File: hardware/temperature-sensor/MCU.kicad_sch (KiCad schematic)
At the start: 43 parts, among them J4 ARM-JTAG-SWD, Q2 DMN3404L, Q3 DMN3404L, Q4 DMN3404L, U1 STM32F407V_E-G_Tx, U4 AT24C512C, Y1 CX2016FB25000C0FZZH1

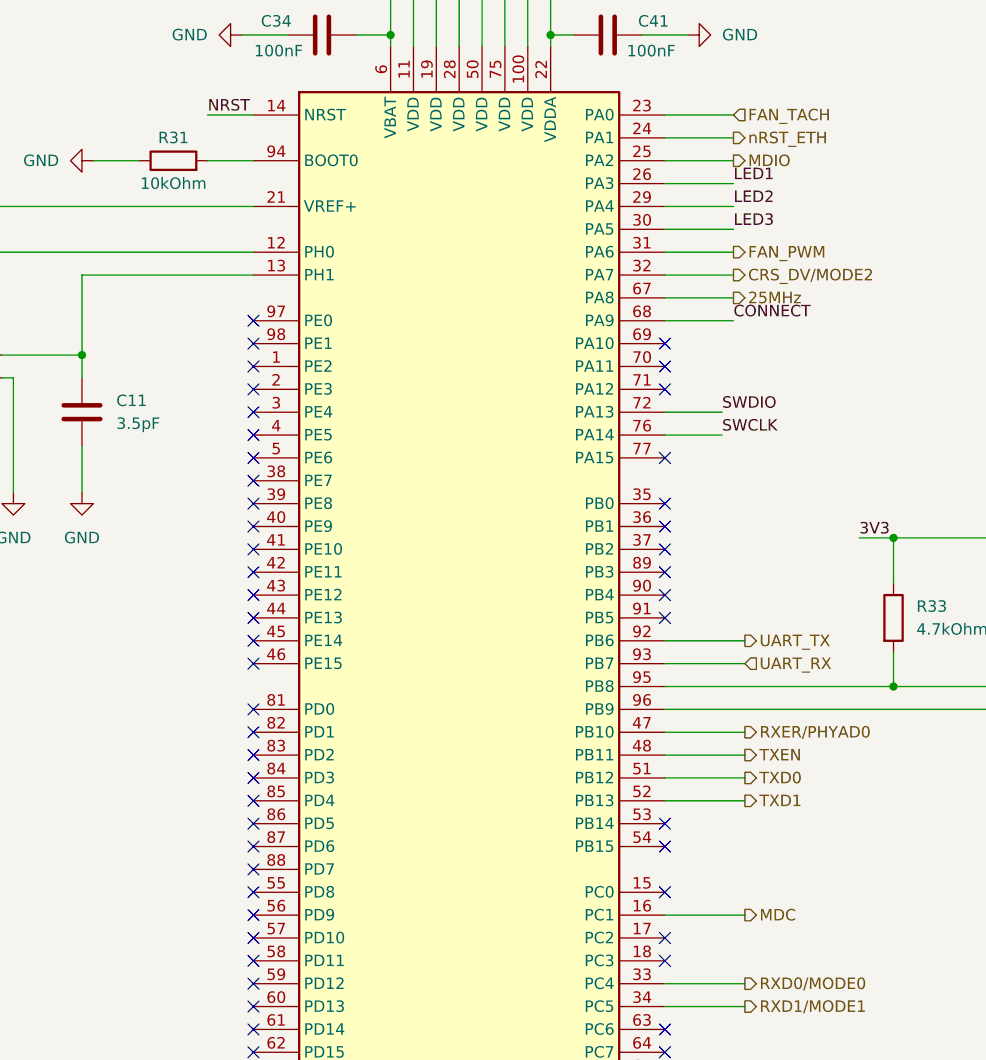
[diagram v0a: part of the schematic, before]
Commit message: add missing routes
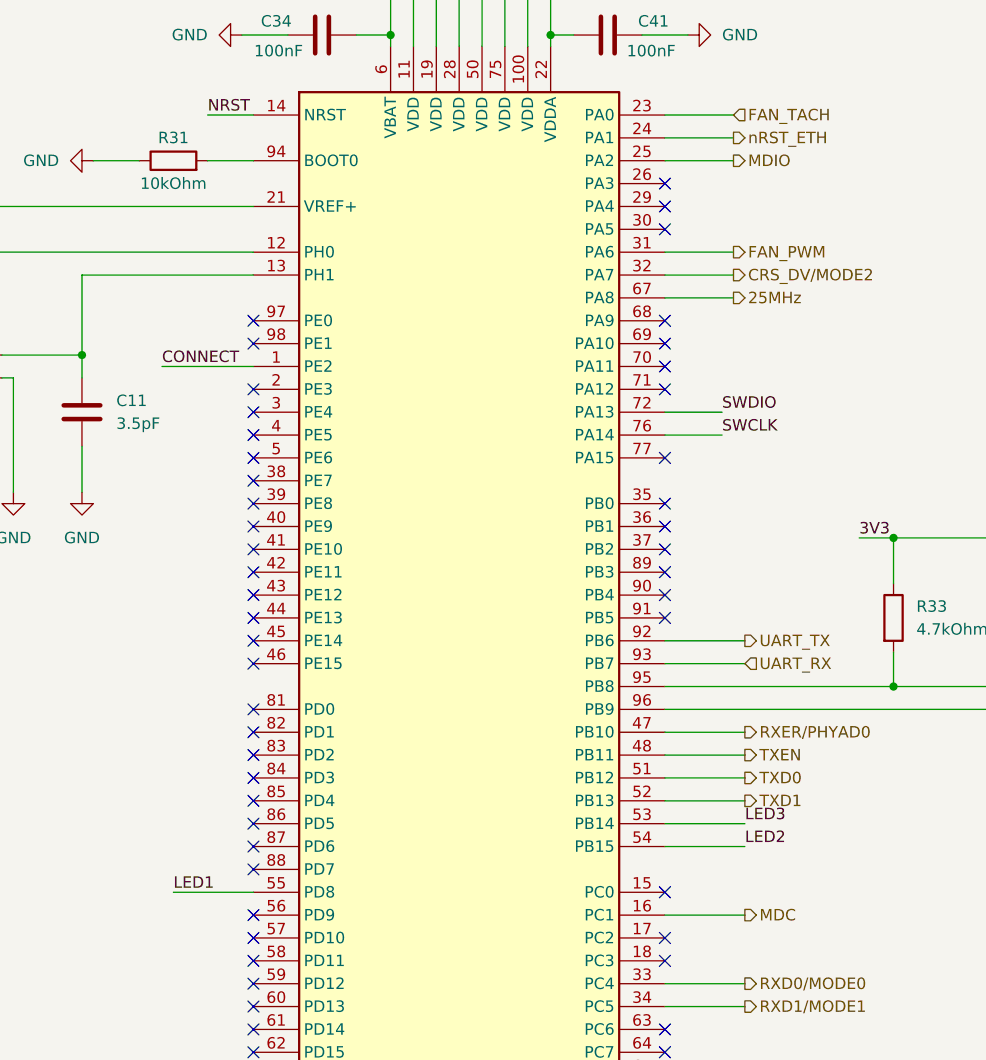
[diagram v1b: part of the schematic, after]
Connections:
- net CONNECT: now also U1.1 (PE2); no longer U1.68 (PA9)
- net LED1: now also U1.55 (PD8); no longer U1.26 (PA3)
- net LED2: now also U1.54 (PB15); no longer U1.29 (PA4)
- net LED3: now also U1.53 (PB14); no longer U1.30 (PA5)
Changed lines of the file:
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@@
+	)
+	(no_connect
+		(at 129.54 62.23)
 	)
 	(no_connect
@@
 	)
 	(no_connect
-		(at 129.54 130.81)
-	)
-	(no_connect
 		(at 129.54 161.29)
 	)
 	(no_connect
-		(at 83.82 138.43)
-	)
-	(no_connect
 		(at 129.54 173.99)
 	)
@@
 	)
 	(no_connect
-		(at 129.54 133.35)
+		(at 129.54 74.93)
 	)
 	(no_connect
@@
 	)
 	(no_connect
-		(at 83.82 80.01)
+		(at 129.54 64.77)
 	)
 	(no_connect
@@
 	)
 	(no_connect
+		(at 129.54 59.69)
+	)
+	(no_connect
 		(at 83.82 146.05)
 	)
@@
 	(wire
 		(pts
-			(xy 129.54 62.23) (xy 137.16 62.23)
-		)
-		(stroke
-			(width 0)
-			(type default)
-		)
-	)
-	(wire
-		(pts
 			(xy 106.68 24.13) (xy 106.68 15.24)
 		)
@@
 	(wire
 		(pts
+			(xy 73.66 80.01) (xy 83.82 80.01)
+		)
+		(stroke
+			(width 0)
+			(type default)
+		)
+	)
+	(wire
+		(pts
 			(xy 49.53 44.45) (xy 49.53 62.23)
 		)
@@
 	(wire
 		(pts
+			(xy 74.93 138.43) (xy 83.82 138.43)
+		)
+		(stroke
+			(width 0)
+			(type default)
+		)
+	)
+	(wire
+		(pts
 			(xy 269.24 137.16) (xy 269.24 139.7)
 		)
@@
 	(wire
 		(pts
+			(xy 129.54 130.81) (xy 138.43 130.81)
+		)
+		(stroke
+			(width 0)
+			(type default)
+		)
+	)
+	(wire
+		(pts
 			(xy 257.81 151.13) (xy 259.08 151.13)
 		)
@@
 	(wire
 		(pts
-			(xy 129.54 59.69) (xy 137.16 59.69)
-		)
-		(stroke
-			(width 0)
-			(type default)
-		)
-	)
-	(wire
-		(pts
 			(xy 196.85 127) (xy 196.85 129.54)
 		)
@@
 	(wire
 		(pts
+			(xy 129.54 133.35) (xy 138.43 133.35)
+		)
+		(stroke
+			(width 0)
+			(type default)
+		)
+	)
+	(wire
+		(pts
 			(xy 17.78 90.17) (xy 17.78 93.98)
 		)
@@
 	(wire
 		(pts
-			(xy 129.54 64.77) (xy 137.16 64.77)
-		)
-		(stroke
-			(width 0)
-			(type default)
-		)
-	)
-	(wire
-		(pts
 			(xy 257.81 144.78) (xy 261.62 144.78)
 		)
@@
 		(pts
 			(xy 233.68 115.57) (xy 233.68 119.38)
-		)
-		(stroke
-			(width 0)
-			(type default)
-		)
-	)
-	(wire
-		(pts
-			(xy 129.54 74.93) (xy 137.16 74.93)
 		)
 		(stroke
@@
 	)
 	(label "CONNECT"
-		(at 137.16 74.93 0)
+		(at 73.66 80.01 0)
 		(effects
 			(font
@@
 	)
 	(label "LED2"
-		(at 137.16 62.23 0)
+		(at 138.43 133.35 0)
 		(effects
 			(font
@@
 	)
 	(label "LED3"
-		(at 137.16 64.77 0)
+		(at 138.43 130.81 0)
 		(effects
 			(font
@@
 	)
 	(label "LED1"
-		(at 137.16 59.69 0)
-		(effects
-			(font
+		(at 74.93 138.43 0)
+		(effects
+			(font

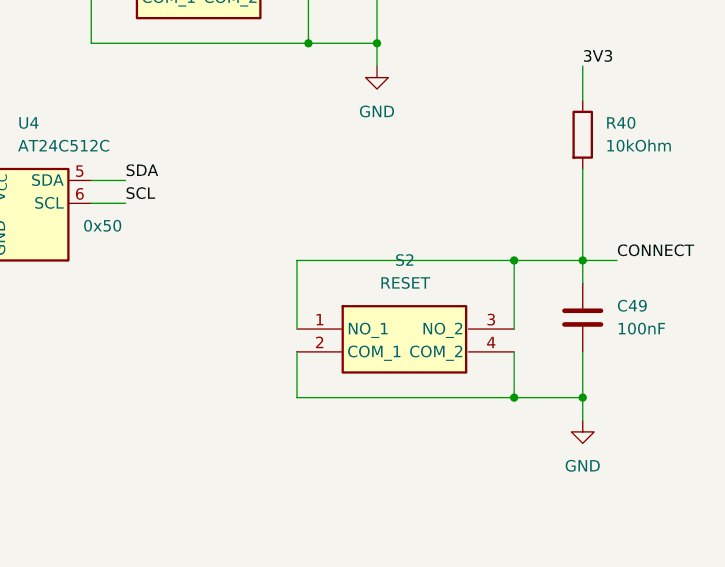
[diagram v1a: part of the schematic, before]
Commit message: fix silkscreen
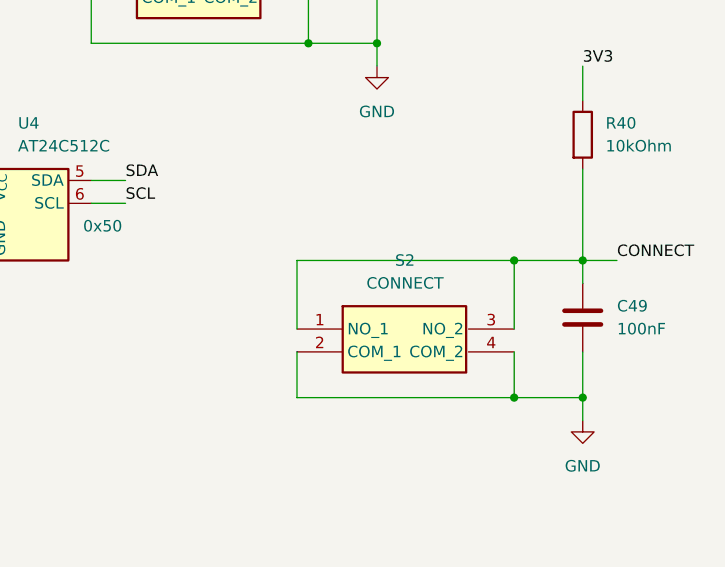
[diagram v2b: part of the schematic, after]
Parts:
- S2: value RESET -> CONNECT
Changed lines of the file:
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@@
 			)
 		)
-		(property "Value" "RESET"
+		(property "Value" "CONNECT"
 			(at 249.4915 81.28 0)
 			(effects
